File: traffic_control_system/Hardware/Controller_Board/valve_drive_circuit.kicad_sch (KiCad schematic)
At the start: 68 parts, among them Q1 BC847, Q2 BC847, Q3 BC847, Q4 BC847, Q5 PMBT3906YS, Q6 PMBT3906YS, Q7 PMBT3906YS, Q8 PMBT3906YS, U1 CPC1114NTR, U2 CPC1114NTR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

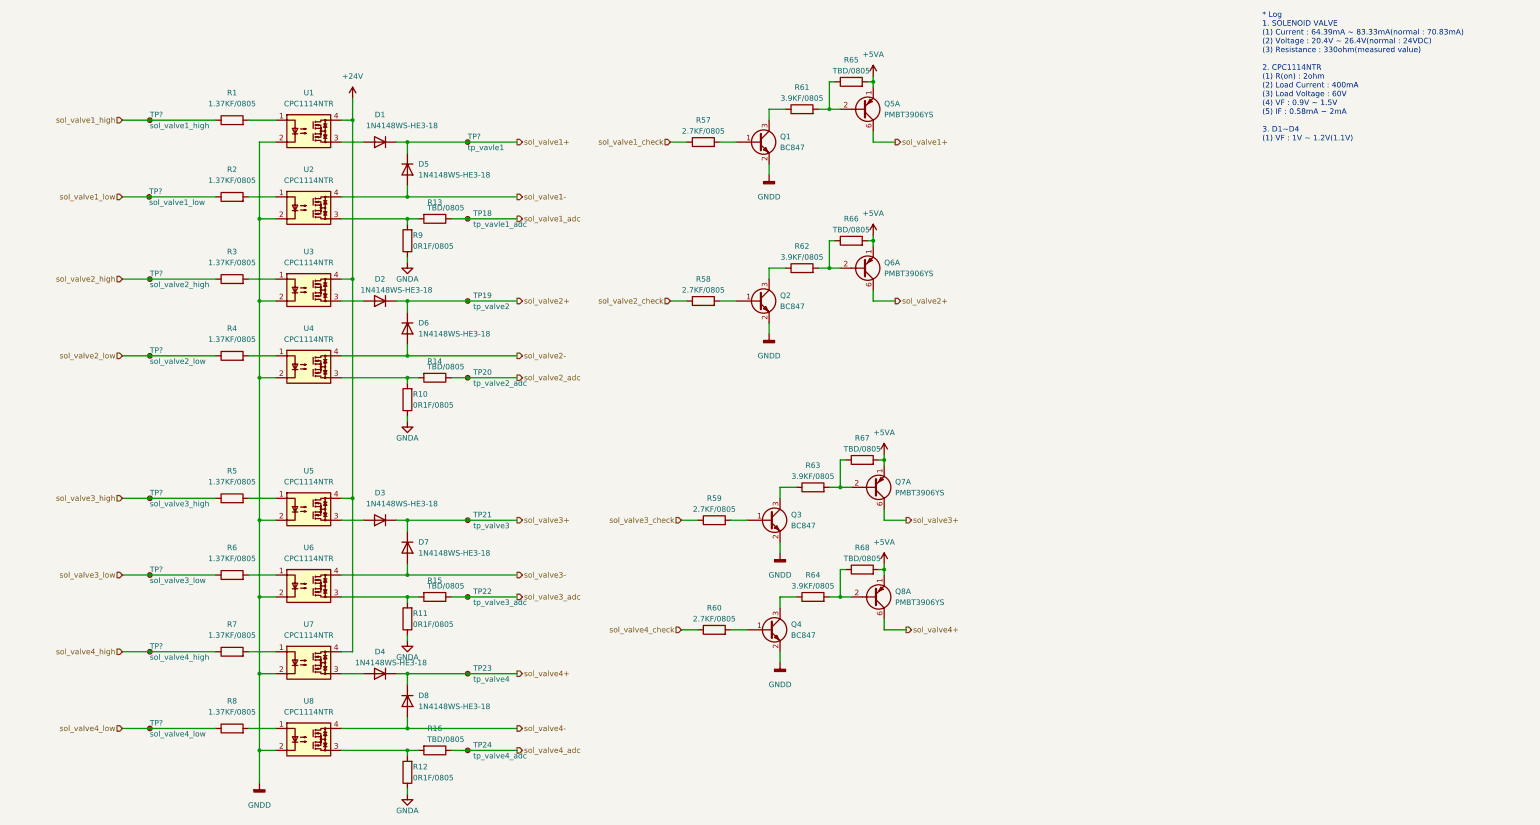
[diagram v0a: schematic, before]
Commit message: issue : 밸브체크 회로 다이오드 누락 추가[ISSUE-6]
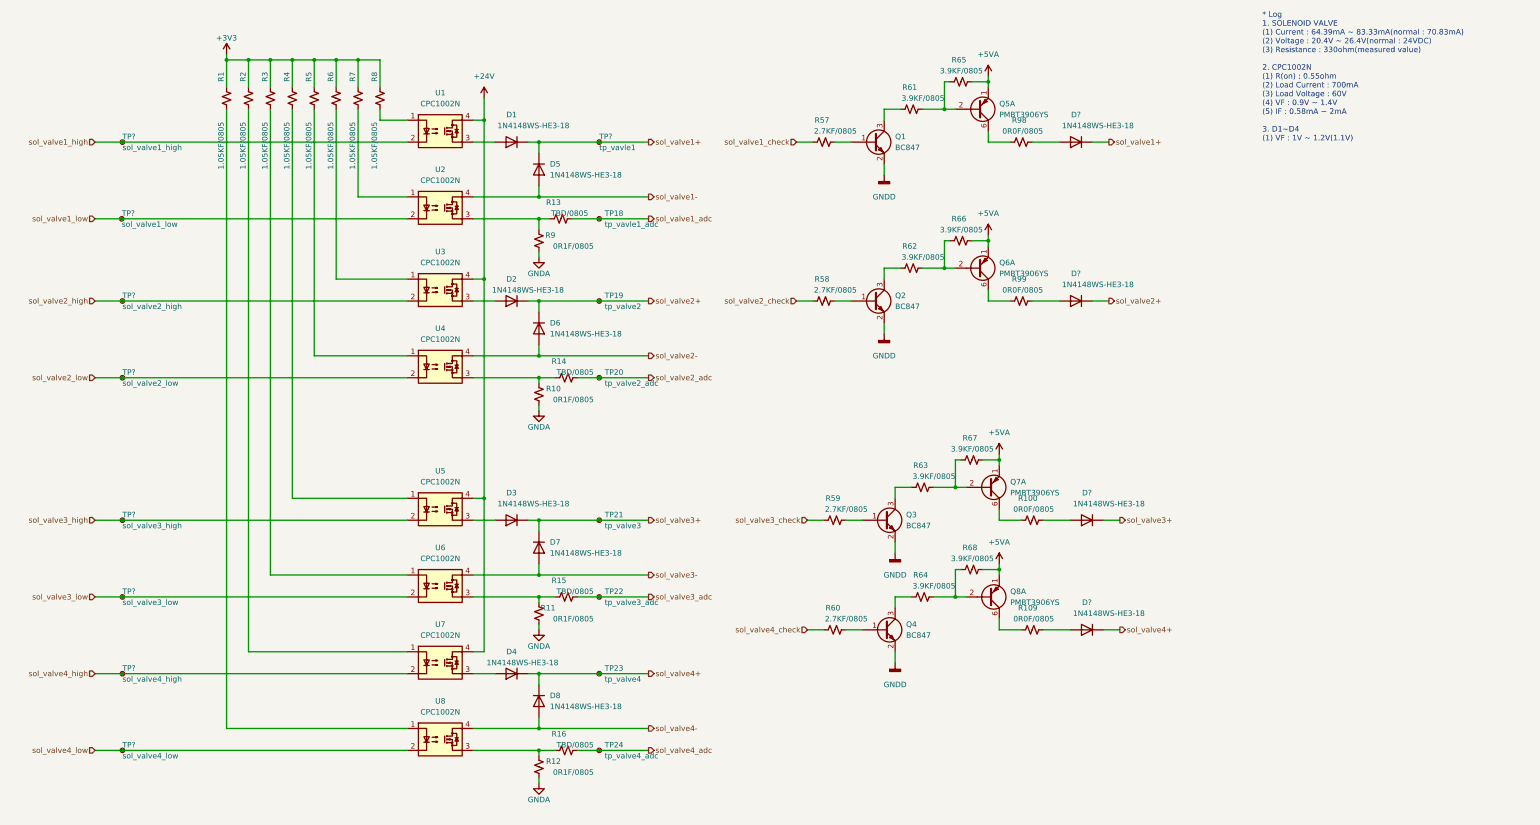
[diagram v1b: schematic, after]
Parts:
- removed R1, R2, R3, R4, R5, R6, R7, R8: 1.37KF/0805, Resistor_SMD:R_0805_2012Metric, symbol Device:R
- removed R10, R11, R12, R9: 0R1F/0805, Resistor_SMD:R_0805_2012Metric, symbol Device:R
- removed R13, R14, R15, R16: TBD/0805, Resistor_SMD:R_0805_2012Metric, symbol Device:R
- removed R57, R58, R59, R60: 2.7KF/0805, symbol Device:R
- removed R61, R62, R63, R64: 3.9KF/0805, symbol Device:R
- removed R65, R66, R67, R68: TBD/0805, symbol Device:R
- removed TP? (x8): tp_vavle1, TestPoint:TestPoint_Pad_D2.5mm, symbol Connector:TestPoint_Small
- removed U1, U2, U3, U4, U5, U6, U7, U8: CPC1114NTR, Package_SO:SOP-4_3.8x4.1mm_P2.54mm, symbol Relay_SolidState:CPC1117N
- added D? (x4): 1N4148WS-HE3-18, Diode_THT:D_DO-35_SOD27_P7.62mm_Horizontal, symbol Diode:1N4148
- added R1, R2, R3, R4, R5, R6, R7, R8: 1.05KF/0805, symbol Device:R_Small_US
- added R10, R11, R12, R9: 0R1F/0805, symbol Device:R_Small_US
- added R100, R109, R98, R99: 0R0F/0805, symbol Device:R_Small_US
- added R13, R14, R15, R16: TBD/0805, symbol Device:R_Small_US
- added R57, R58, R59, R60: 2.7KF/0805, symbol Device:R_Small_US
- added R61, R62, R63, R64, R65, R66, R67, R68: 3.9KF/0805, symbol Device:R_Small_US
- added TP? (x8): tp_vavle1, TestPoint:TestPoint_Pad_D2.5mm, symbol Connector:TestPoint_Small
- added U1, U2, U3, U4, U5, U6, U7, U8: CPC1002N, Package_SO:SOP-4_3.8x4.1mm_P2.54mm, symbol Relay_SolidState:CPC1002N
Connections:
- net +24V: now also U1.4, U3.4, U5.4, U7.4
- net +5VA: now also R65.1, R66.1, R67.1, R68.1
- net GNDA: now also R10.2, R11.2, R12.2, R9.2
- net sol_valve1+: now also D?.1 (K); no longer Q5.6 (C1)
- net sol_valve1-: now also U2.4
- net sol_valve1_adc: now also R13.1
- net sol_valve1_check: now also R57.2
- net sol_valve1_high: now also TP?.1, U1.2
- net sol_valve1_low: now also TP?.1, U2.2
- net sol_valve2+: now also D?.1 (K); no longer Q6.6 (C1)
- net sol_valve2-: now also U4.4
- net sol_valve2_adc: now also R14.1
- net sol_valve2_check: now also R58.2
- net sol_valve2_high: now also TP?.1, U3.2
- net sol_valve2_low: now also TP?.1, U4.2
- net sol_valve3+: now also D?.1 (K); no longer Q7.6 (C1)
- net sol_valve3-: now also U6.4
- net sol_valve3_adc: now also R15.1
- net sol_valve3_check: now also R59.2
- net sol_valve3_high: now also TP?.1, U5.2
- net sol_valve3_low: now also TP?.1, U6.2
- net sol_valve4+: now also D?.1 (K); no longer Q8.6 (C1)
- net sol_valve4-: now also U8.4
- net sol_valve4_adc: now also R16.1
- net sol_valve4_check: now also R60.2
- net sol_valve4_high: now also TP?.1, U7.2
- net sol_valve4_low: now also TP?.1, U8.2
- net at Q3.3 (C): now also R63.2
- net at Q7.2 (B1): now also R63.1, R67.2
- net at D2.2 (A): now also U3.3
- net at D3.2 (A): now also U5.3
- net at Q2.1 (B): now also R58.1
- net at Q2.3 (C): now also R62.2
- net at Q3.1 (B): now also R59.1
- net at Q1.1 (B): now also R57.1
- net at Q8.2 (B1): now also R64.1, R68.2
- net at Q1.3 (C): now also R61.2
- net at D1.2 (A): now also U1.3
- net at D4.2 (A): now also U7.3
- net at Q5.2 (B1): now also R61.1, R65.2
- net at Q4.1 (B): now also R60.1
- net at Q4.3 (C): now also R64.2
- net at Q6.2 (B1): now also R62.1, R66.2
- new net: R8.1, U1.1
- new net: R12.1, R16.2, U8.3
- new net: D?.2 (A), R98.1
- new net: Q5.6 (C1), R98.2
- new net: R5.1, U4.1
- new net: D?.2 (A), R100.1
- new net: Q7.6 (C1), R100.2
- new net: R7.1, U2.1
- new net: R13.2, R9.1, U2.3
- new net: D?.2 (A), R109.1
- new net: D?.2 (A), R99.1
- new net: R10.1, R14.2, U4.3
- new net: R11.1, R15.2, U6.3
- new net: R3.1, U6.1
- new net: R2.1, U7.1
- new net: R1.1, U8.1
- new net: R4.1, U5.1
- new net: Q8.6 (C1), R109.2
- new net: Q6.6 (C1), R99.2
- new net: R6.1, U3.1
- new net +3V3: R1.2, R2.2, R3.2, R4.2, R5.2, R6.2, R7.2, R8.2
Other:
- note added: "* Log 1. SOLENOID VALVE (1) Current : 64.39mA ~ 83.33mA(normal : 70.83mA) (2) Voltage : 20.4V ~ 26.4V(normal : 24VDC) (3) Resistance : 330ohm(measured value) 2. CPC1002N (1) R(on) : 0.55ohm (2) Load Current : 700mA (3) Load Voltage : 60V (4) VF : 0.9V ~ 1.4V (5) IF : 0.58mA ~ 2mA 3. D1~D4 (1) VF : 1V ~ 1.2V(1.1V)"
- note removed: "* Log 1. SOLENOID VALVE (1) Current : 64.39mA ~ 83.33mA(normal : 70.83mA) (2) Voltage : 20.4V ~ 26.4V(normal : 24VDC) (3) Resistance : 330ohm(measured value) 2. CPC1114NTR (1) R(on) : 2ohm (2) Load Current : 400mA (3) Load Voltage : 60V (4) VF : 0.9V ~ 1.5V (5) IF : 0.58mA ~ 2mA 3. D1~D4 (1) VF : 1V ~ 1.2V(1.1V)"
- moved on the sheet: D1, D2, D3, D4, D5, D6, D7, D8, Q1, Q2, Q3, Q4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

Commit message: issue : 깃 커밋 히스토리 정리를 위한 원본 저장소의 브랜치 분리 작업[TRAFFIC-CONTROL6]
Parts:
- R10, R11, R12, R9: P/N (none) -> LR2512-22R010F4
- gave numbers to parts that had none: 4
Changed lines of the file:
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@@
   (title_block
     (title "Valve_Drive_Circuit")
-    (date "2022-07-03")
-    (rev "rev02")
+    (date "2022-07-12")
+    (rev "rev03")
   )
   (junction (at 133.35 125.73) (diameter 0) (color 0 0 0 0)
@@
       (effects (font (size 1.27 1.27)) hide)
     )
+    (property "P/N" "LR2512-22R010F4" (id 4) (at 133.35 182.88 0)
+      (effects (font (size 1.27 1.27)) hide)
+    )
     (pin "1")
     (pin "2")
@@
   (symbol (lib_id "Diode:1N4148") (at 260.35 151.13 180) (unit 1)
     (in_bom yes) (on_board yes)
-    (property "Reference" "D?" (id 0) (at 260.35 144.78 0))
+    (property "Reference" "D20" (id 0) (at 260.35 144.78 0))
     (property "Value" "1N4148WS-HE3-18" (id 1) (at 265.43 147.32 0))
     (property "Footprint" "Diode_THT:D_DO-35_SOD27_P7.62mm_Horizontal" (id 2) (at 260.35 146.685 0)
@@
   (symbol (lib_id "Diode:1N4148") (at 257.81 74.93 180) (unit 1)
     (in_bom yes) (on_board yes)
-    (property "Reference" "D?" (id 0) (at 257.81 68.58 0))
+    (property "Reference" "D18" (id 0) (at 257.81 68.58 0))
     (property "Value" "1N4148WS-HE3-18" (id 1) (at 262.89 71.12 0))
     (property "Footprint" "Diode_THT:D_DO-35_SOD27_P7.62mm_Horizontal" (id 2) (at 257.81 70.485 0)
@@
   (symbol (lib_id "Diode:1N4148") (at 260.35 125.73 180) (unit 1)
     (in_bom yes) (on_board yes)
-    (property "Reference" "D?" (id 0) (at 260.35 119.38 0))
+    (property "Reference" "D19" (id 0) (at 260.35 119.38 0))
     (property "Value" "1N4148WS-HE3-18" (id 1) (at 265.43 121.92 0))
     (property "Footprint" "Diode_THT:D_DO-35_SOD27_P7.62mm_Horizontal" (id 2) (at 260.35 121.285 0)
@@
   (symbol (lib_id "Diode:1N4148") (at 257.81 38.1 180) (unit 1)
     (in_bom yes) (on_board yes)
-    (property "Reference" "D?" (id 0) (at 257.81 31.75 0))
+    (property "Reference" "D17" (id 0) (at 257.81 31.75 0))
     (property "Value" "1N4148WS-HE3-18" (id 1) (at 262.89 34.29 0))
     (property "Footprint" "Diode_THT:D_DO-35_SOD27_P7.62mm_Horizontal" (id 2) (at 257.81 33.655 0)
@@
       (effects (font (size 1.27 1.27)) hide)
     )
+    (property "P/N" "LR2512-22R010F4" (id 4) (at 133.35 147.32 0)
+      (effects (font (size 1.27 1.27)) hide)
+    )
     (pin "1")
     (pin "2")
@@
       (effects (font (size 1.27 1.27)) hide)
     )
+    (property "P/N" "LR2512-22R010F4" (id 4) (at 133.35 60.96 0)
+      (effects (font (size 1.27 1.27)) hide)
+    )
     (pin "1")
     (pin "2")
@@
       (effects (font (size 1.27 1.27)) hide)
     )
+    (property "P/N" "LR2512-22R010F4" (id 4) (at 133.35 96.52 0)
+      (effects (font (size 1.27 1.27)) hide)
+    )
